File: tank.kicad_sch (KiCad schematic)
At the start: 1 part, among them J1 USB4230-03-A_REVA

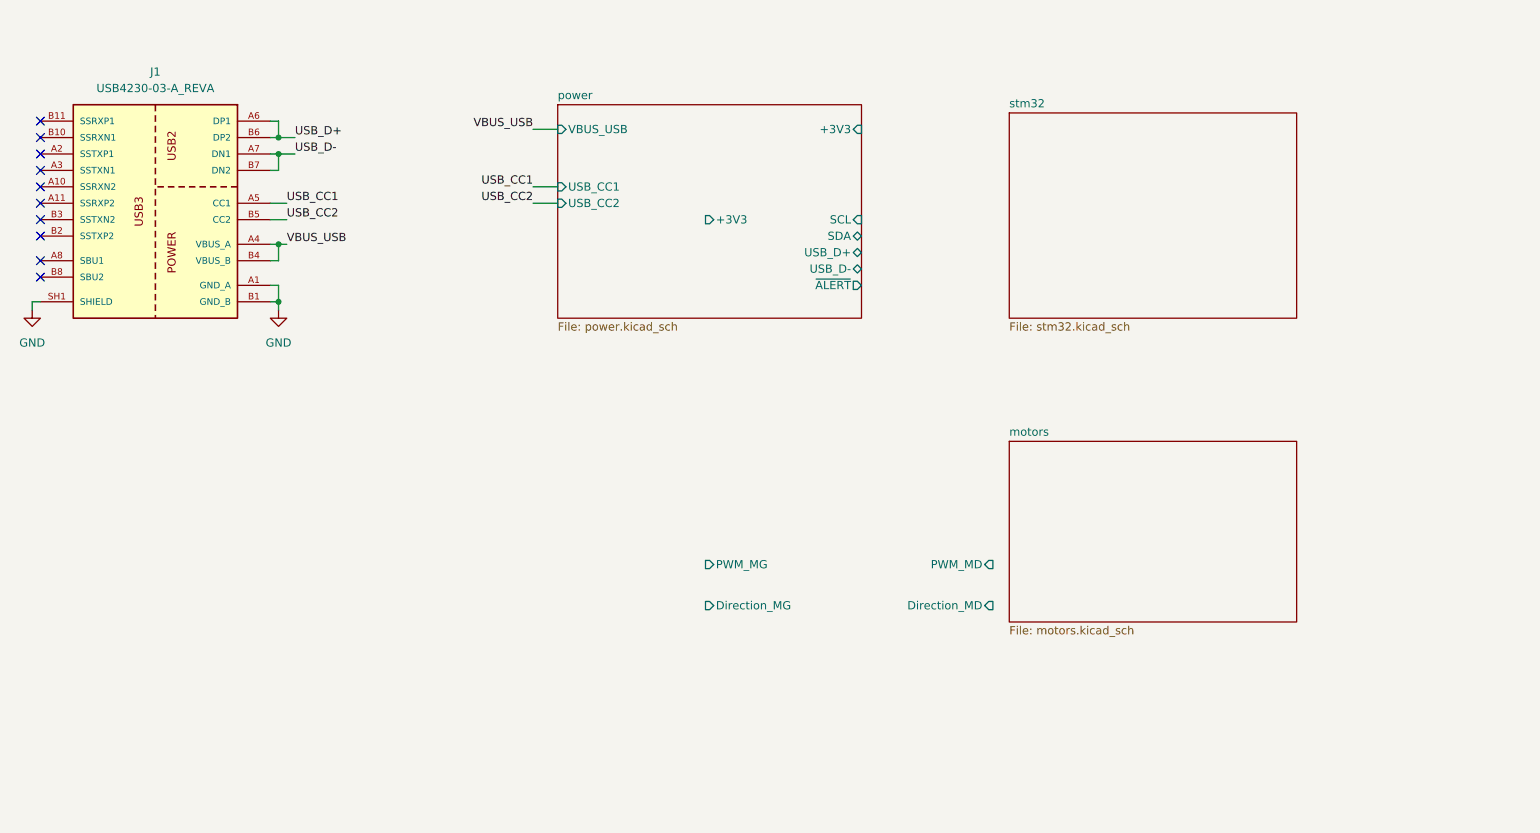
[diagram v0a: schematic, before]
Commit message: Version 0. Schémas finalisés. Mise à jour des résistances en série E12. Réduction de la BOM.
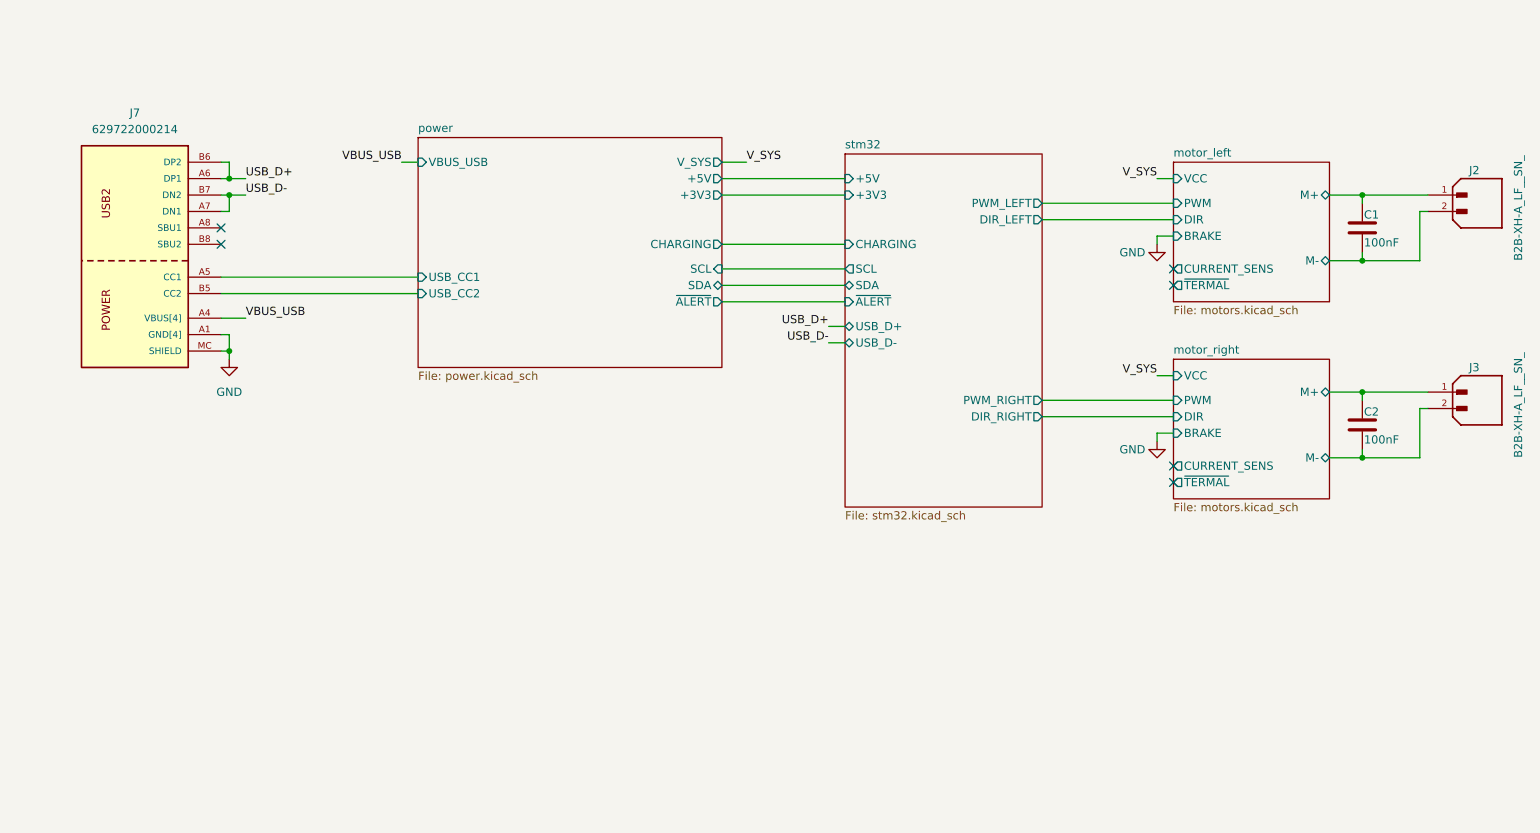
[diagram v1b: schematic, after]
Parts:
- removed J1: USB4230-03-A_REVA, local:GCT_USB4230-03-A_REVA, symbol local:USB4230-03-A_REVA
- added C1, C2: 100nF, Capacitor_SMD:C_0805_2012Metric, symbol local:C_0402
- added J2, J3: B2B-XH-A_LF__SN_, local:JST_B2B-XH-A_LF__SN_, symbol local:B2B-XH-A_LF__SN_
- added J7: 629722000214, local:629722000214, symbol local:629722000214
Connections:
- net GND: now also J7.A1 (GND[4]), J7.A12 (GND[4]), J7.B1 (GND[4]), J7.B12 (GND[4]), J7.MC (SHIELD), J7.S2, J7.S3, J7.S4
- net USB_D+: now also J7.A6 (DP1), J7.B6 (DP2)
- net USB_D-: now also J7.A7 (DN1), J7.B7 (DN2)
- new net VBUS_USB: J7.A4 (VBUS[4]), J7.A9 (VBUS[4]), J7.B4 (VBUS[4]), J7.B9 (VBUS[4])
- new net motor_left/M+: C1.1, J2.1
- new net motor_left/M-: C1.2, J2.2
- new net motor_right/M+: C2.1, J3.1
- new net motor_right/M-: C2.2, J3.2
- new net power/USB_CC1: J7.A5 (CC1)
- new net power/USB_CC2: J7.B5 (CC2)
- no-connect marks 10 -> 6
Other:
- sheet motors renamed motor_left
- added sheet motor_right (motors.kicad_sch)
- sheet motor_left ports: added BRAKE, CURRENT_SENS, DIR, M+, M-, PWM, VCC, ~{TERMAL}; removed Direction_MD, Direction_MG, PWM_MD, PWM_MG
- sheet power ports: added +5V, CHARGING, V_SYS; removed USB_D+, USB_D-
- sheet stm32 ports: added +5V, CHARGING, DIR_LEFT, DIR_RIGHT, PWM_LEFT, PWM_RIGHT, SCL, SDA, USB_D+, USB_D-, ~{ALERT}; removed none

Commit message: Minor Schematics update
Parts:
- added J4: Conn_ENC_LEFT, Connector_PinHeader_2.54mm:PinHeader_1x04_P2.54mm_Vertical, symbol Connector:Conn_01x04_Pin
- added J5: Conn_ENC_RIGHT, Connector_PinHeader_2.54mm:PinHeader_1x04_P2.54mm_Vertical, symbol Connector:Conn_01x04_Pin
- added R1, R2, R5, R6: 2.7k, Resistor_SMD:R_0603_1608Metric, symbol local:R
- added R3, R4, R7, R8: 4.7k, Resistor_SMD:R_0603_1608Metric, symbol local:R
- C1, C2: footprint Capacitor_SMD:C_0805_2012Metric -> Capacitor_SMD:C_0603_1608Metric; symbol local:C_0402 -> local:C
- renumbered J7 to J1
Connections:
- net GND: now also J1.S1 (SHIELD), J4.4 (Pin_4), J5.4 (Pin_4), R3.2, R4.2, R7.2, R8.2; no longer J1.MC (SHIELD)
- new net: J4.2 (Pin_2), R1.2
- new net: J5.2 (Pin_2), R5.2
- new net: J5.3 (Pin_3), R6.2
- new net: J4.3 (Pin_3), R2.2
- new net +5V: J4.1 (Pin_1), J5.1 (Pin_1)
- new net ENC_A_LEFT: R1.1, R3.1
- new net ENC_A_RIGHT: R5.1, R7.1
- new net ENC_B_LEFT: R2.1, R4.1
- new net ENC_B_RIGHT: R6.1, R8.1
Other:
- sheet stm32 ports: added ENC_A_LEFT, ENC_A_RIGHT, ENC_B_LEFT, ENC_B_RIGHT; removed none
- moved on the sheet: C1, C2, J1, J2, J3

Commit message: Modification mineur du schéma, ajout du PCB V1
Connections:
- net +5V: now also J4.4 (Pin_4), J5.4 (Pin_4); no longer J4.1 (Pin_1), J5.1 (Pin_1)
- net GND: now also J4.1 (Pin_1), J5.1 (Pin_1); no longer J4.4 (Pin_4), J5.4 (Pin_4)
- net motor_left/M+: now also C2.1, J3.1; no longer C1.1, J2.1
- net motor_left/M-: now also C2.2, J3.2; no longer C1.2, J2.2
- net motor_right/M+: now also C1.1, J2.1; no longer C2.1, J3.1
- net motor_right/M-: now also C1.2, J2.2; no longer C2.2, J3.2
- net at R1.2: now also J4.3 (Pin_3); no longer J4.2 (Pin_2)
- net at R5.2: now also J5.3 (Pin_3); no longer J5.2 (Pin_2)
- net at R6.2: now also J5.2 (Pin_2); no longer J5.3 (Pin_3)
- net at R2.2: now also J4.2 (Pin_2); no longer J4.3 (Pin_3)
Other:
- moved on the sheet: C1, C2, J2, J3

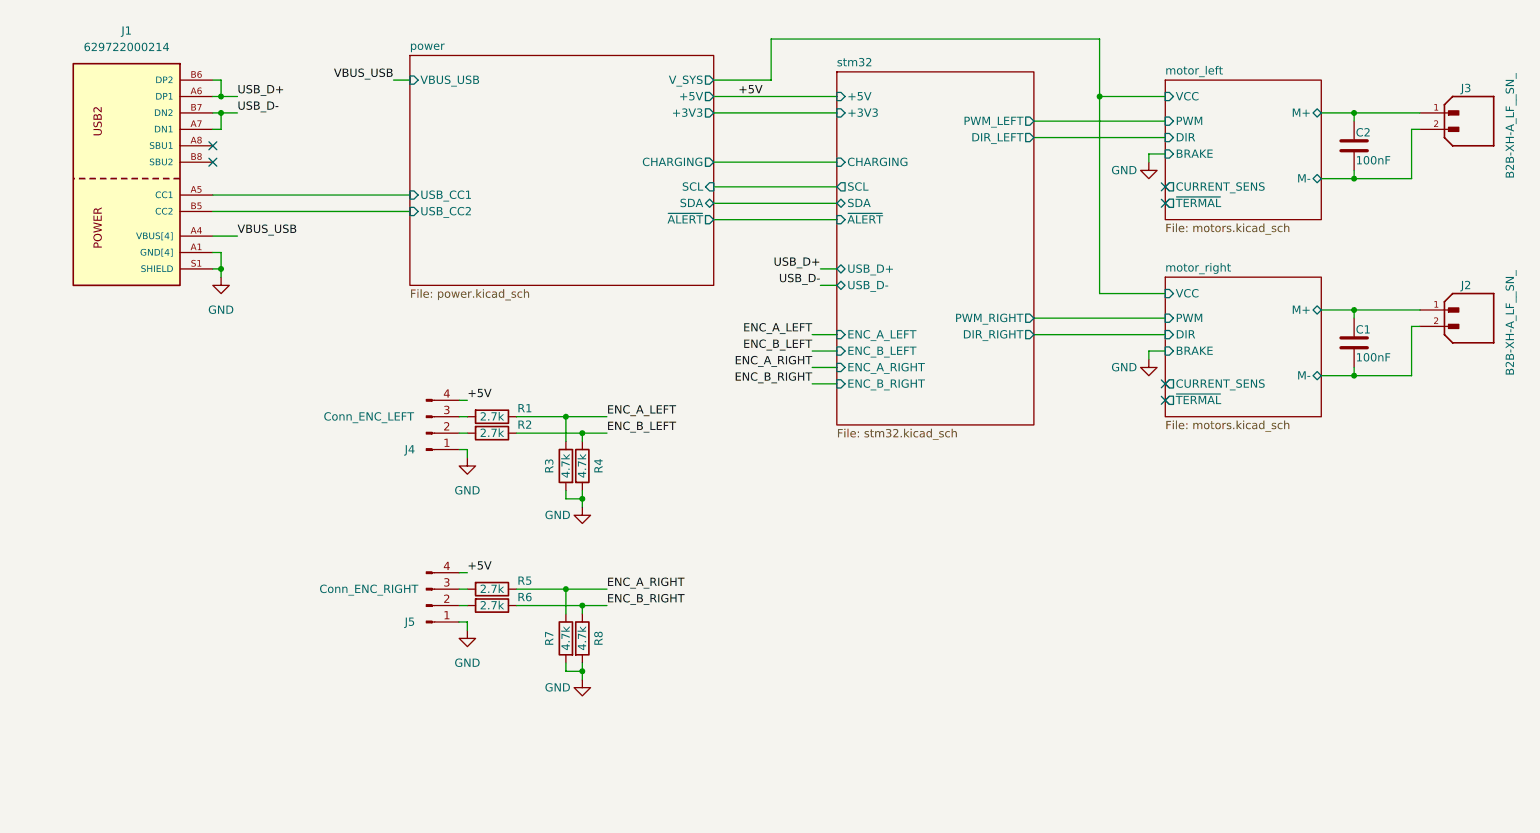
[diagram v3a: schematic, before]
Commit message: Modifications mineurs du schéma. Passage sous Kicad 10 ok. Finalisations PCB (teardrops, arrondis)
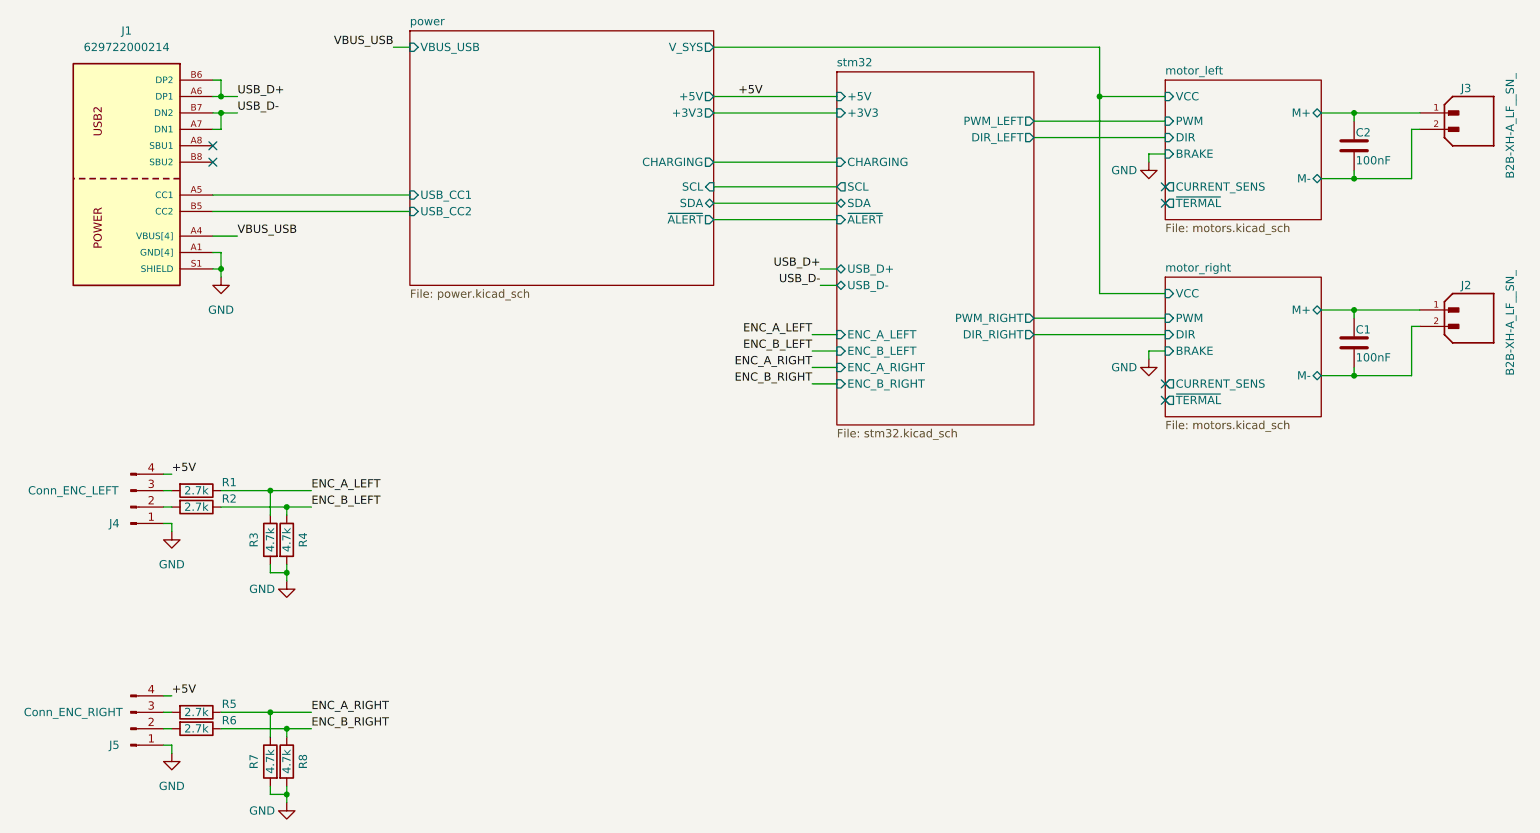
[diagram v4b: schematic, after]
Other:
- moved on the sheet: J4, J5, R1, R2, R3, R4, R5, R6, R7, R8
